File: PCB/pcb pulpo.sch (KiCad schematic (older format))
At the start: 48 parts, among them J1 fan1, J10 fan8, J11 fan8, J12 izq, J13 dcha, J2 Entrada 12V, J3 fan2, J4 fan3, J5 fan4, J6 fan5, J7 fan6, J8 fan7, J9 fan8, Q1 IRF540N, Q10 IRF540N, Q2 IRF540N, Q3 IRF540N, Q4 IRF540N, Q5 IRF540N, Q6 IRF540N, Q7 IRF540N, Q8 IRF540N, Q9 IRF540N, U1 Teensy3.0, U2 LM7805_TO220

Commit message: Boceto PCB
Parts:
- J12, J13: footprint (none) -> Connector_PinSocket_2.54mm:PinSocket_1x14_P2.54mm_Vertical
- J14: renamed from J?; footprint (none) -> Connector_PinSocket_2.54mm:PinSocket_1x05_P2.54mm_Vertical
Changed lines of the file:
@@
 F 0 "J12" H 5677 2826 50  0000 L CNN
 F 1 "izq" H 5677 2735 50  0000 L CNN
-F 2 "" H 5650 2850 50  0001 C CNN
+F 2 "Connector_PinSocket_2.54mm:PinSocket_1x14_P2.54mm_Vertical" H 5650 2850 50  0001 C CNN
 F 3 "~" H 5650 2850 50  0001 C CNN
 	1    5650 2850
@@
 F 0 "J13" H 5544 3975 50  0000 C CNN
 F 1 "dcha" H 5544 4066 50  0000 C CNN
-F 2 "" H 5650 4900 50  0001 C CNN
+F 2 "Connector_PinSocket_2.54mm:PinSocket_1x14_P2.54mm_Vertical" H 5650 4900 50  0001 C CNN
 F 3 "~" H 5650 4900 50  0001 C CNN
 	1    5650 4900
@@
 	9350 3550 8950 3550
 $Comp
-L Connector:Conn_01x05_Female J?
+L Connector:Conn_01x05_Female J14
 U 1 1 5C2E0A99
 P 6000 3850
-F 0 "J?" H 5894 4235 50  0000 C CNN
+F 0 "J14" H 5894 4235 50  0000 C CNN
 F 1 "inf" H 5894 4144 50  0000 C CNN
-F 2 "" H 6000 3850 50  0001 C CNN
+F 2 "Connector_PinSocket_2.54mm:PinSocket_1x05_P2.54mm_Vertical" H 6000 3850 50  0001 C CNN
 F 3 "~" H 6000 3850 50  0001 C CNN
 	1    6000 3850

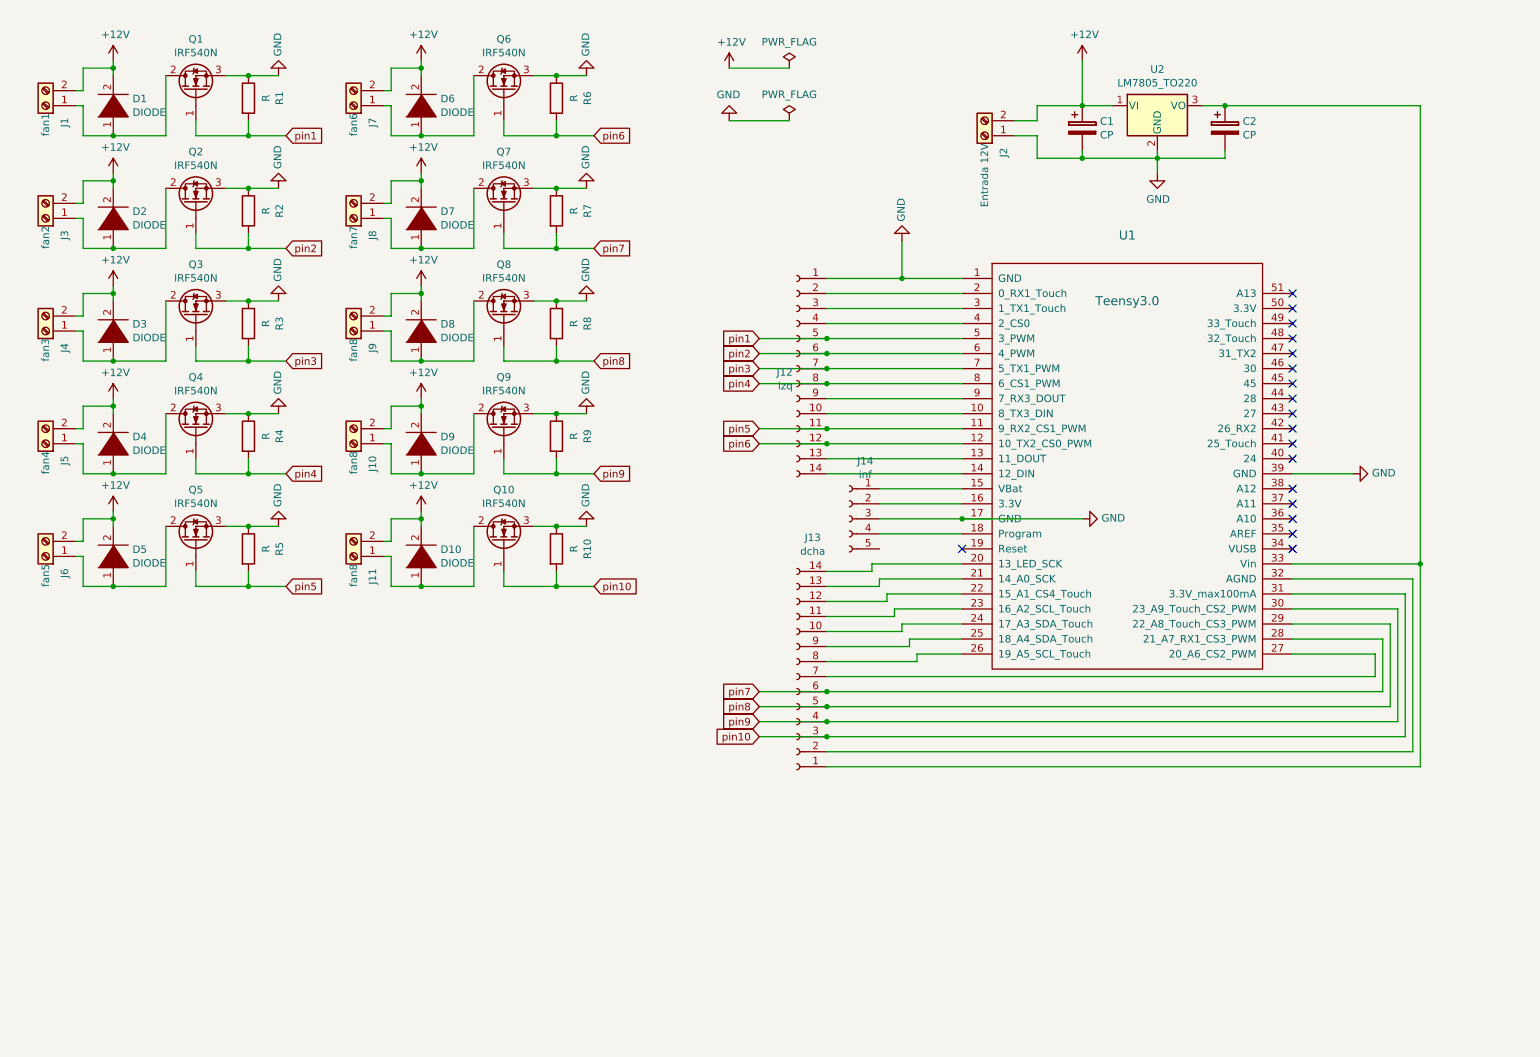
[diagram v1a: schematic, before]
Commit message: añadidos leds a la placa y junta para la cabeza
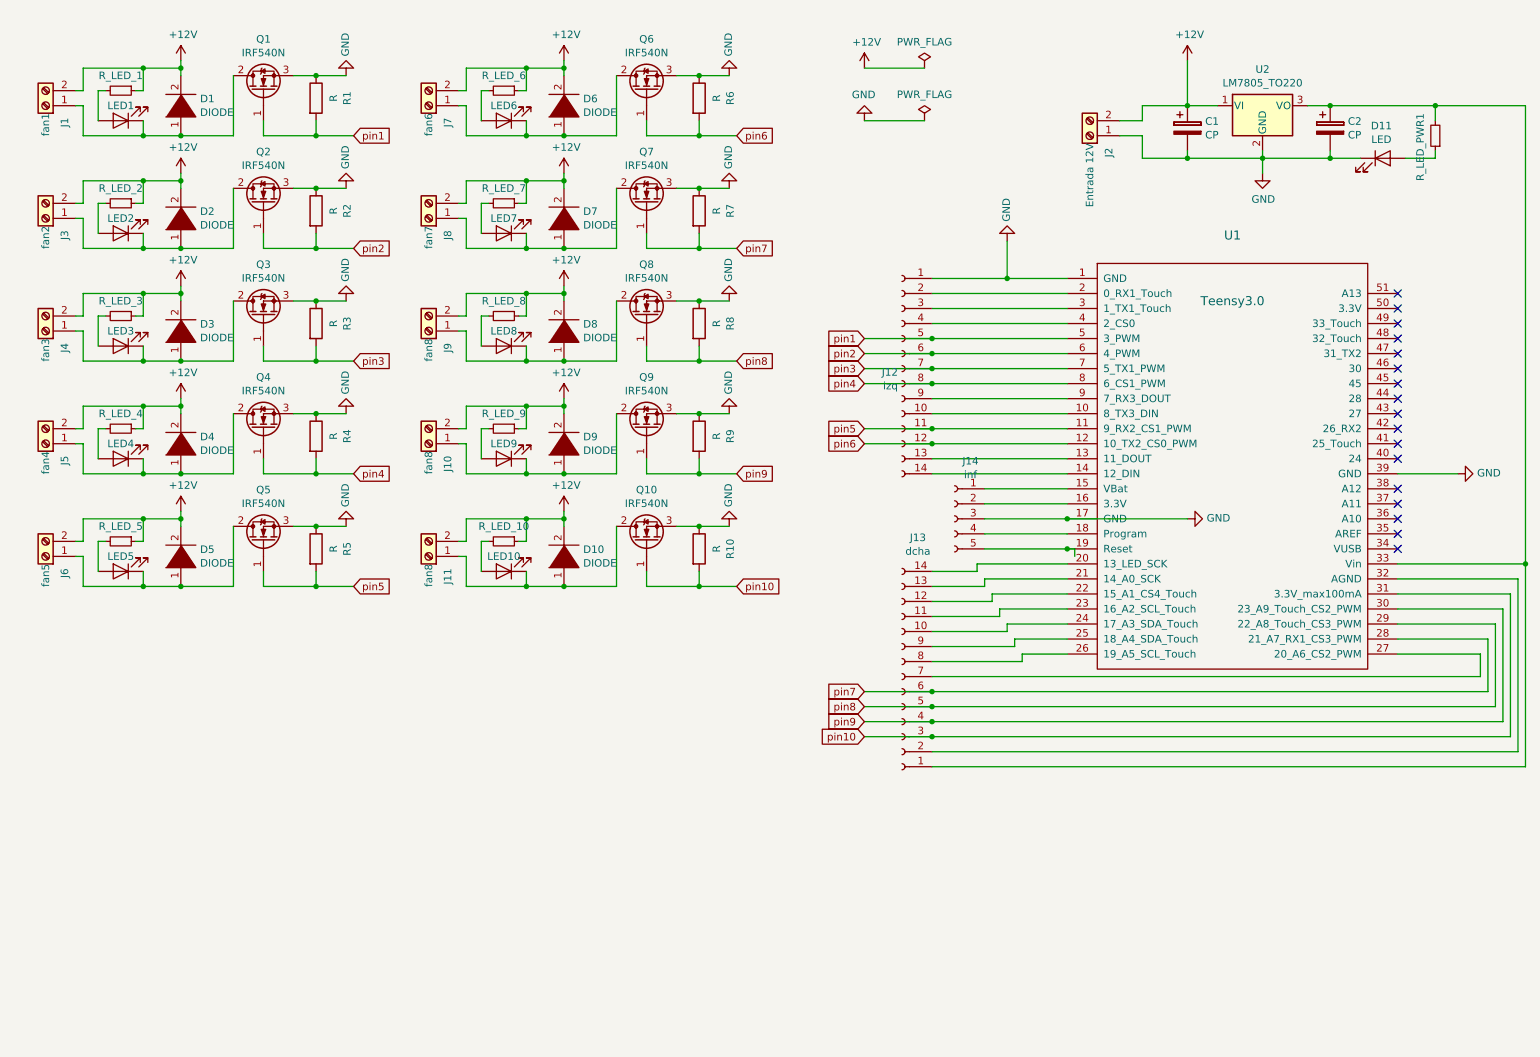
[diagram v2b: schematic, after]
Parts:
- added D11, LED1, LED10, LED2, LED3, LED4, LED5, LED6, LED7, LED8, LED9: LED, LED_THT:LED_D3.0mm, symbol Device:LED
- added R_LED_1, R_LED_10, R_LED_2, R_LED_3, R_LED_4, R_LED_5, R_LED_6, R_LED_7, R_LED_8, R_LED_9: R_LED, Resistor_THT:R_Axial_DIN0204_L3.6mm_D1.6mm_P2.54mm_Vertical, symbol Device:R_Small
- added R_LED_PWR1: R_Small, Resistor_THT:R_Axial_DIN0204_L3.6mm_D1.6mm_P2.54mm_Vertical, symbol Device:R_Small
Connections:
- net +12V: now also R_LED_1.1, R_LED_10.1, R_LED_2.1, R_LED_3.1, R_LED_4.1, R_LED_5.1, R_LED_6.1, R_LED_7.1, R_LED_8.1, R_LED_9.1
- net GND: now also D11.1 (K)
- net at D1.1 (K), J1.1 (Pin_1), Q1.2 (D): now also LED1.1 (K)
- net at U1.19 (Reset): now also J14.5 (Pin_5)
- net at C2.1, J13.1 (Pin_1), U1.33 (Vin)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: now also R_LED_PWR1.2
- net at D2.1 (K), J3.1 (Pin_1), Q2.2 (D): now also LED2.1 (K)
- net at D3.1 (K), J4.1 (Pin_1), Q3.2 (D): now also LED3.1 (K)
- net at D4.1 (K), J5.1 (Pin_1), Q4.2 (D): now also LED4.1 (K)
- net at D5.1 (K), J6.1 (Pin_1), Q5.2 (D): now also LED5.1 (K)
- net at D6.1 (K), J7.1 (Pin_1), Q6.2 (D): now also LED6.1 (K)
- net at D7.1 (K), J8.1 (Pin_1), Q7.2 (D): now also LED7.1 (K)
- net at D8.1 (K), J9.1 (Pin_1), Q8.2 (D): now also LED8.1 (K)
- net at D9.1 (K), J10.1 (Pin_1), Q9.2 (D): now also LED9.1 (K)
- net at D10.1 (K), J11.1 (Pin_1), Q10.2 (D): now also LED10.1 (K)
- new net: D11.2 (A), R_LED_PWR1.1
- new net: LED1.2 (A), R_LED_1.2
- new net: LED2.2 (A), R_LED_2.2
- new net: LED3.2 (A), R_LED_3.2
- new net: LED4.2 (A), R_LED_4.2
- new net: LED5.2 (A), R_LED_5.2
- new net: LED10.2 (A), R_LED_10.2
- new net: LED9.2 (A), R_LED_9.2
- new net: LED8.2 (A), R_LED_8.2
- new net: LED7.2 (A), R_LED_7.2
- new net: LED6.2 (A), R_LED_6.2
- no-connect marks 18 -> 17
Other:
- moved on the sheet: C1, C2, D1, D10, D2, D3, D4, D5, D6, D7, D8, D9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

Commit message: Cambio posición LEDs a antes del MOSFET y revisión de estilo en el esquema
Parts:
- removed D1, D10, D2, D3, D4, D5, D6, D7, D8, D9: DIODE, Diode_THT:D_DO-34_SOD68_P10.16mm_Horizontal, symbol pspice:DIODE
- removed J1: fan1, TerminalBlock:TerminalBlock_bornier-2_P5.08mm, symbol Connector:Screw_Terminal_01x02
- removed LED1: LED, LED_THT:LED_D3.0mm, symbol Device:LED
- removed Q1, Q10, Q2, Q3, Q5, Q6, Q7, Q8, Q9: IRF540N, Package_TO_SOT_THT:TO-220-3_Vertical, symbol Transistor_FET:IRF540N
- removed R1: R, Resistor_THT:R_Axial_DIN0207_L6.3mm_D2.5mm_P10.16mm_Horizontal, symbol Device:R
- removed R_LED_1, R_LED_10, R_LED_2, R_LED_3, R_LED_4, R_LED_5, R_LED_6, R_LED_7, R_LED_8, R_LED_9: R_LED, Resistor_THT:R_Axial_DIN0204_L3.6mm_D1.6mm_P2.54mm_Vertical, symbol Device:R_Small
- added D1, D10, D2, D3, D4, D5, D6, D7, D8, D9: 1N4004, Diode_THT:D_DO-41_SOD81_P10.16mm_Horizontal, symbol Diode:1N4004
- added J5: fan4, TerminalBlock:TerminalBlock_bornier-2_P5.08mm, symbol Connector:Screw_Terminal_01x02
- added LED4: LED, LED_THT:LED_D3.0mm, symbol Device:LED
- added MOS_10, MOS_2, MOS_3, MOS_4, MOS_5, MOS_6, MOS_7, MOS_8, MOS_9: RFP50N06, Package_TO_SOT_THT:TO-220-3_Vertical, symbol Transistor_FET:IRF540N
- added R4: 10K, Resistor_THT:R_Axial_DIN0207_L6.3mm_D2.5mm_P10.16mm_Horizontal, symbol Device:R
- added R_LED_1, R_LED_10, R_LED_2, R_LED_3, R_LED_4, R_LED_5, R_LED_6, R_LED_7, R_LED_8, R_LED_9: 330R, Resistor_THT:R_Axial_DIN0207_L6.3mm_D2.5mm_P10.16mm_Horizontal, symbol Device:R
- J1: renamed from J5; value fan4 -> fan1
- J10: value fan8 -> fan9
- J11: value fan8 -> fan10
- MOS_1: renamed from Q4; value IRF540N -> RFP50N06
- R1: renamed from R4; value R -> 10K
- R10, R2, R3, R5, R6, R7, R8, R9: value R -> 10K
- U1: symbol teensy:Teensy3.0 -> pcb-pulpo-rescue:Teensy3.0-teensy
- renumbered LED4 to LED1, D11 to PWR_LED1
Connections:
- net +12V: now also J1.1 (Pin_1), J10.1 (Pin_1), J11.1 (Pin_1), J2.1 (Pin_1), J3.1 (Pin_1), J4.1 (Pin_1), J6.1 (Pin_1), J7.1 (Pin_1), J8.1 (Pin_1), J9.1 (Pin_1), D1.1 (K), D10.1 (K), D2.1 (K), D3.1 (K), D4.1 (K), D5.1 (K), D6.1 (K), D7.1 (K), D8.1 (K), D9.1 (K), J5.1 (Pin_1); no longer J1.2 (Pin_2), J10.2 (Pin_2), J11.2 (Pin_2), J2.2 (Pin_2), J3.2 (Pin_2), J4.2 (Pin_2), J6.2 (Pin_2), J7.2 (Pin_2), J8.2 (Pin_2), J9.2 (Pin_2)
- net GND: now also J2.2 (Pin_2), LED1.1 (K), LED10.1 (K), LED2.1 (K), LED3.1 (K), LED5.1 (K), LED6.1 (K), LED7.1 (K), LED8.1 (K), LED9.1 (K), R1.2, R10.2, R2.2, R3.2, R5.2, R6.2, R7.2, R8.2, R9.2, LED4.1 (K), MOS_10.3 (S), MOS_2.3 (S), MOS_3.3 (S), MOS_4.3 (S), MOS_5.3 (S), MOS_6.3 (S), MOS_7.3 (S), MOS_8.3 (S), MOS_9.3 (S), R4.2; no longer J2.1 (Pin_1), R1.1, R10.1, R2.1, R3.1, R5.1, R6.1, R7.1, R8.1, R9.1
- net pin1: now also MOS_1.1 (G), R1.1, R_LED_1.1; no longer J12.5 (Pin_5), U1.5 (3_PWM)
- net pin10: now also R10.1, MOS_10.1 (G), R_LED_10.1; no longer R10.2
- net pin2: now also R2.1, MOS_2.1 (G), R_LED_2.1; no longer J12.6 (Pin_6), R2.2, U1.6 (4_PWM)
- net pin3: now also R3.1, MOS_3.1 (G), R_LED_3.1; no longer J12.7 (Pin_7), R3.2, U1.7 (5_TX1_PWM)
- net pin4: now also MOS_4.1 (G), R4.1, R_LED_4.1; no longer J12.8 (Pin_8), MOS_1.1 (G), R1.2, U1.8 (6_CS1_PWM)
- net pin5: now also R5.1, MOS_5.1 (G), R_LED_5.1; no longer J12.11 (Pin_11), R5.2, U1.11 (9_RX2_CS1_PWM)
- net pin6: now also R6.1, MOS_6.1 (G), R_LED_6.1; no longer J12.12 (Pin_12), R6.2, U1.12 (10_TX2_CS0_PWM)
- net pin7: now also R7.1, MOS_7.1 (G), R_LED_7.1; no longer R7.2
- net pin8: now also R8.1, MOS_8.1 (G), R_LED_8.1; no longer R8.2
- net pin9: now also R9.1, MOS_9.1 (G), R_LED_9.1; no longer R9.2
- net at LED2.2 (A): now also R_LED_2.2
- net at LED3.2 (A): now also R_LED_3.2
- net at LED1.2 (A): now also R_LED_1.2
- net at LED5.2 (A): now also R_LED_5.2
- net at LED10.2 (A): now also R_LED_10.2
- net at LED9.2 (A): now also R_LED_9.2
- net at LED8.2 (A): now also R_LED_8.2
- net at LED7.2 (A): now also R_LED_7.2
- net at LED6.2 (A): now also R_LED_6.2
- new net: J12.11 (Pin_11), U1.11 (9_RX2_CS1_PWM)
- new net: J12.12 (Pin_12), U1.12 (10_TX2_CS0_PWM)
- new net: J12.5 (Pin_5), U1.5 (3_PWM)
- new net: J12.6 (Pin_6), U1.6 (4_PWM)
- new net: J12.7 (Pin_7), U1.7 (5_TX1_PWM)
- new net: J12.8 (Pin_8), U1.8 (6_CS1_PWM)
- new net: D1.2 (A), J1.2 (Pin_2), MOS_1.2 (D)
- new net: D2.2 (A), J3.2 (Pin_2), MOS_2.2 (D)
- new net: D3.2 (A), J4.2 (Pin_2), MOS_3.2 (D)
- new net: LED4.2 (A), R_LED_4.2
- new net: D4.2 (A), J5.2 (Pin_2), MOS_4.2 (D)
- new net: D5.2 (A), J6.2 (Pin_2), MOS_5.2 (D)
- new net: D6.2 (A), J7.2 (Pin_2), MOS_6.2 (D)
- new net: D7.2 (A), J8.2 (Pin_2), MOS_7.2 (D)
- new net: D8.2 (A), J9.2 (Pin_2), MOS_8.2 (D)
- new net: D9.2 (A), J10.2 (Pin_2), MOS_9.2 (D)
- new net: D10.2 (A), J11.2 (Pin_2), MOS_10.2 (D)
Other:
- moved on the sheet: C1, C2, J2, LED1, PWR_LED1

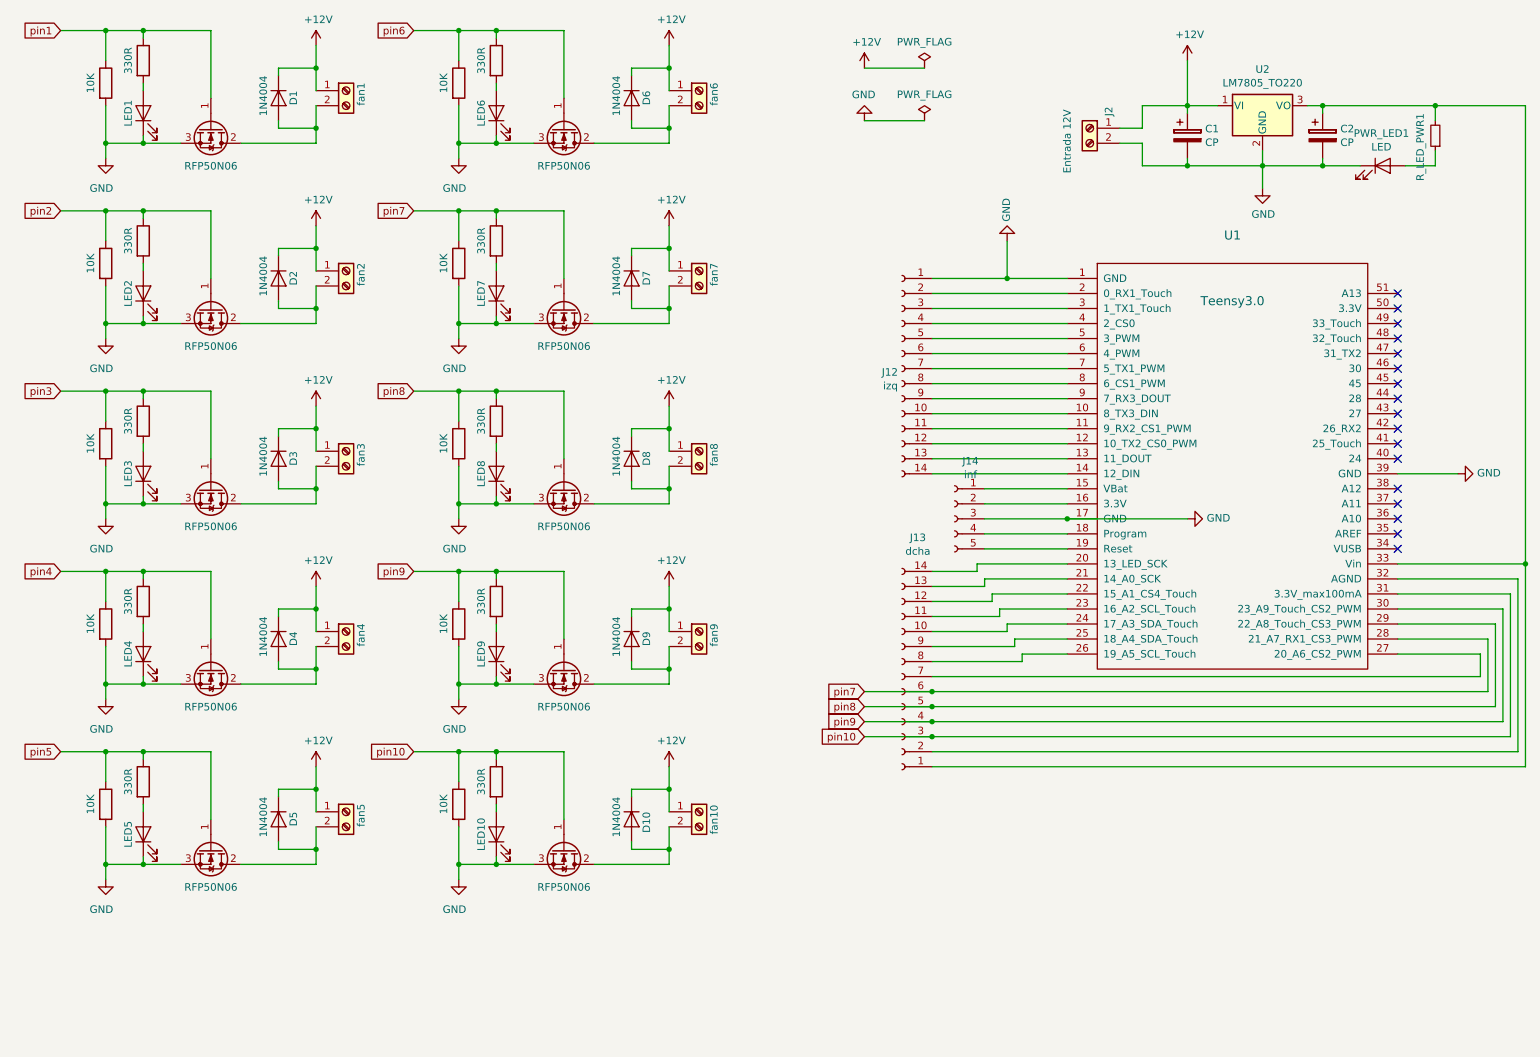
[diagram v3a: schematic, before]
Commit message: mejoras en componentes
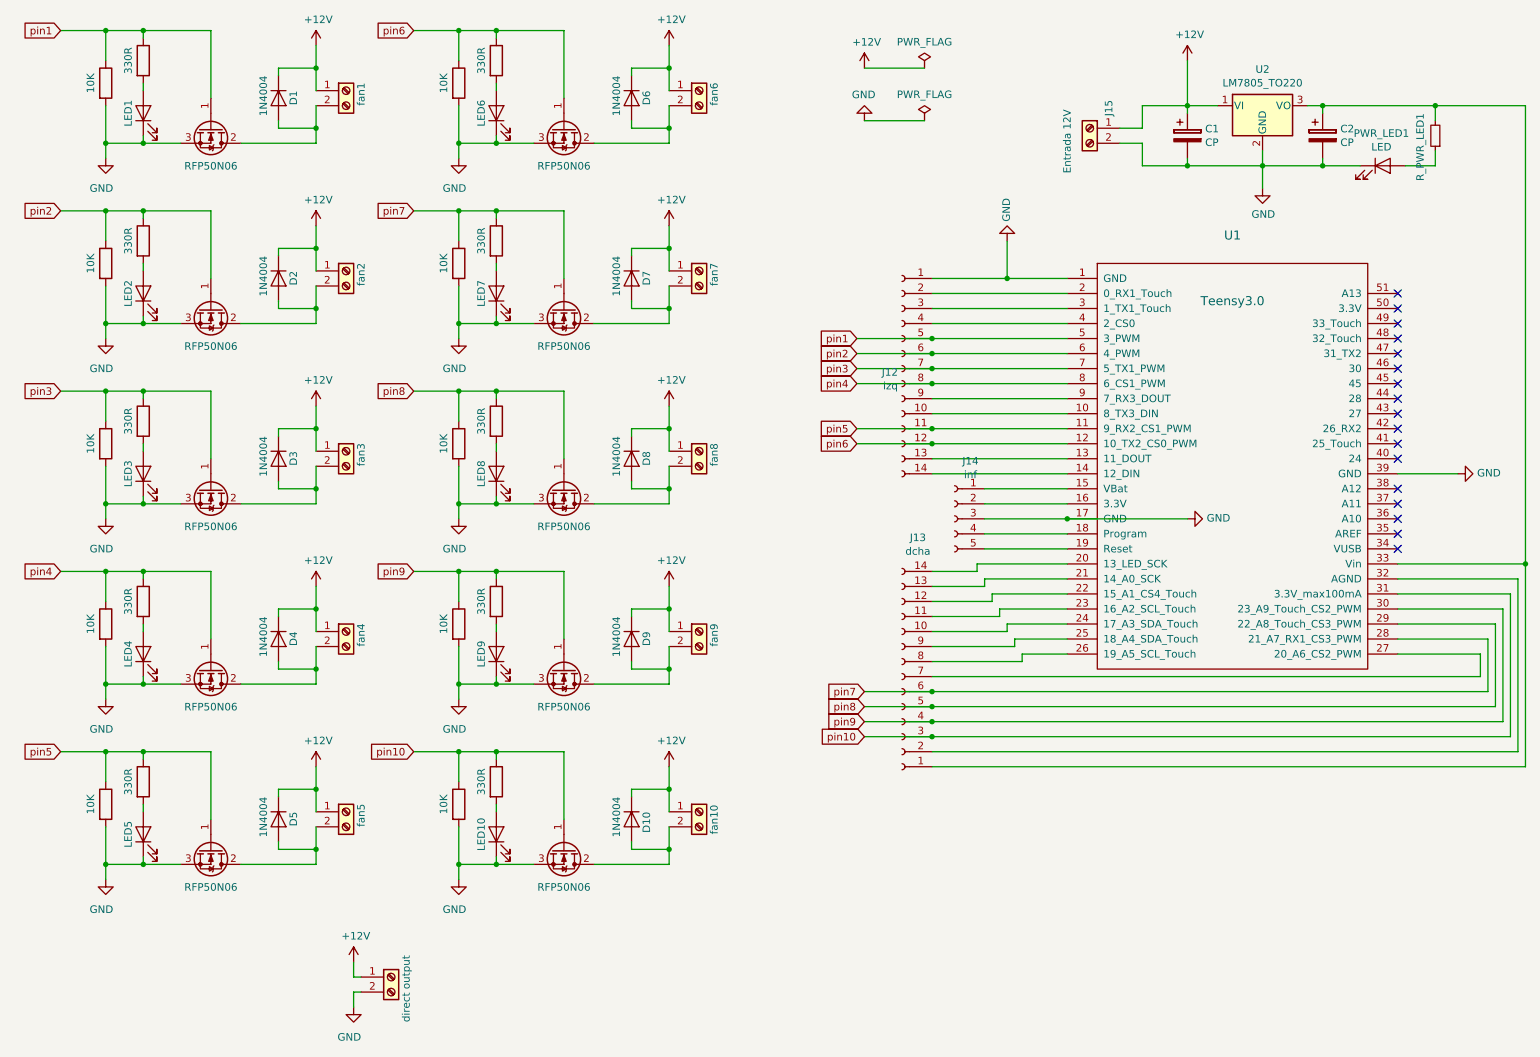
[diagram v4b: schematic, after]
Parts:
- added J6: direct output, TerminalBlock:TerminalBlock_bornier-2_P5.08mm, symbol Connector:Screw_Terminal_01x02
- C1, C2: footprint Capacitor_THT:CP_Axial_L10.0mm_D6.0mm_P15.00mm_Horizontal -> Capacitor_THT:CP_Radial_D10.0mm_P3.80mm
- renumbered J2 to J15, J3 to J2, J4 to J3, J5 to J4, J6 to J5, R_LED_PWR1 to R_PWR_LED1
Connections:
- net +12V: now also J6.1 (Pin_1)
- net GND: now also J6.2 (Pin_2)
- net pin1: now also J12.5 (Pin_5), U1.5 (3_PWM)
- net pin2: now also J12.6 (Pin_6), U1.6 (4_PWM)
- net pin3: now also J12.7 (Pin_7), U1.7 (5_TX1_PWM)
- net pin4: now also J12.8 (Pin_8), U1.8 (6_CS1_PWM)
- net pin5: now also J12.11 (Pin_11), U1.11 (9_RX2_CS1_PWM)
- net pin6: now also J12.12 (Pin_12), U1.12 (10_TX2_CS0_PWM)

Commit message: cambios en la pcb. añadido footprint conector Pablo. Falta cambiar algunos componentes y routear
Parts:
- C1, C2: footprint Capacitor_THT:CP_Radial_D10.0mm_P3.80mm -> Capacitor_THT:CP_Radial_D6.3mm_P2.50mm
- J15: footprint TerminalBlock:TerminalBlock_bornier-2_P5.08mm -> teensy:conector pablo pulpo hinchoshwi
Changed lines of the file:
@@
 F 0 "J15" V 7473 1330 50  0000 L CNN
 F 1 "Entrada 12V" V 7750 950 50  0000 L CNN
-F 2 "TerminalBlock:TerminalBlock_bornier-2_P5.08mm" H 7600 1250 50  0001 C CNN
+F 2 "teensy:conector pablo pulpo hinchoshwi" H 7600 1250 50  0001 C CNN
 F 3 "~" H 7600 1250 50  0001 C CNN
 	1    7600 1250
@@
 F 0 "C1" H 8368 1346 50  0000 L CNN
 F 1 "CP" H 8368 1255 50  0000 L CNN
-F 2 "Capacitor_THT:CP_Radial_D10.0mm_P3.80mm" H 8288 1150 50  0001 C CNN
+F 2 "Capacitor_THT:CP_Radial_D6.3mm_P2.50mm" H 8288 1150 50  0001 C CNN
 F 3 "~" H 8250 1300 50  0001 C CNN
 	1    8250 1300
@@
 F 0 "C2" H 9268 1346 50  0000 L CNN
 F 1 "CP" H 9268 1255 50  0000 L CNN
-F 2 "Capacitor_THT:CP_Radial_D10.0mm_P3.80mm" H 9188 1150 50  0001 C CNN
+F 2 "Capacitor_THT:CP_Radial_D6.3mm_P2.50mm" H 9188 1150 50  0001 C CNN
 F 3 "~" H 9150 1300 50  0001 C CNN
 	1    9150 1300
